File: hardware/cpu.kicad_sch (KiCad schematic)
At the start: 8 parts, among them U1 H3

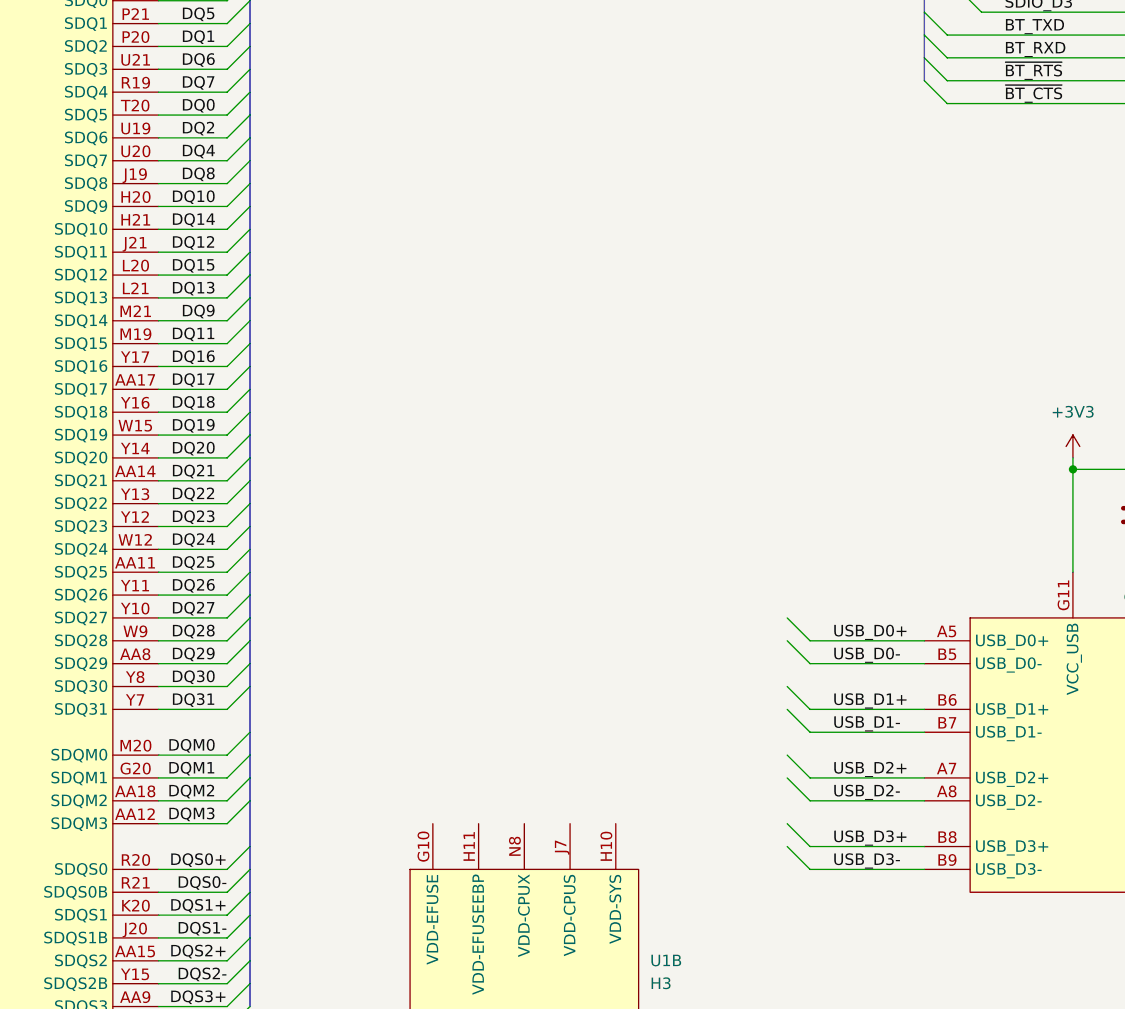
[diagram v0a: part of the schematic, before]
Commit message: Re-routed DDR3 on L4 & drew USB schematic
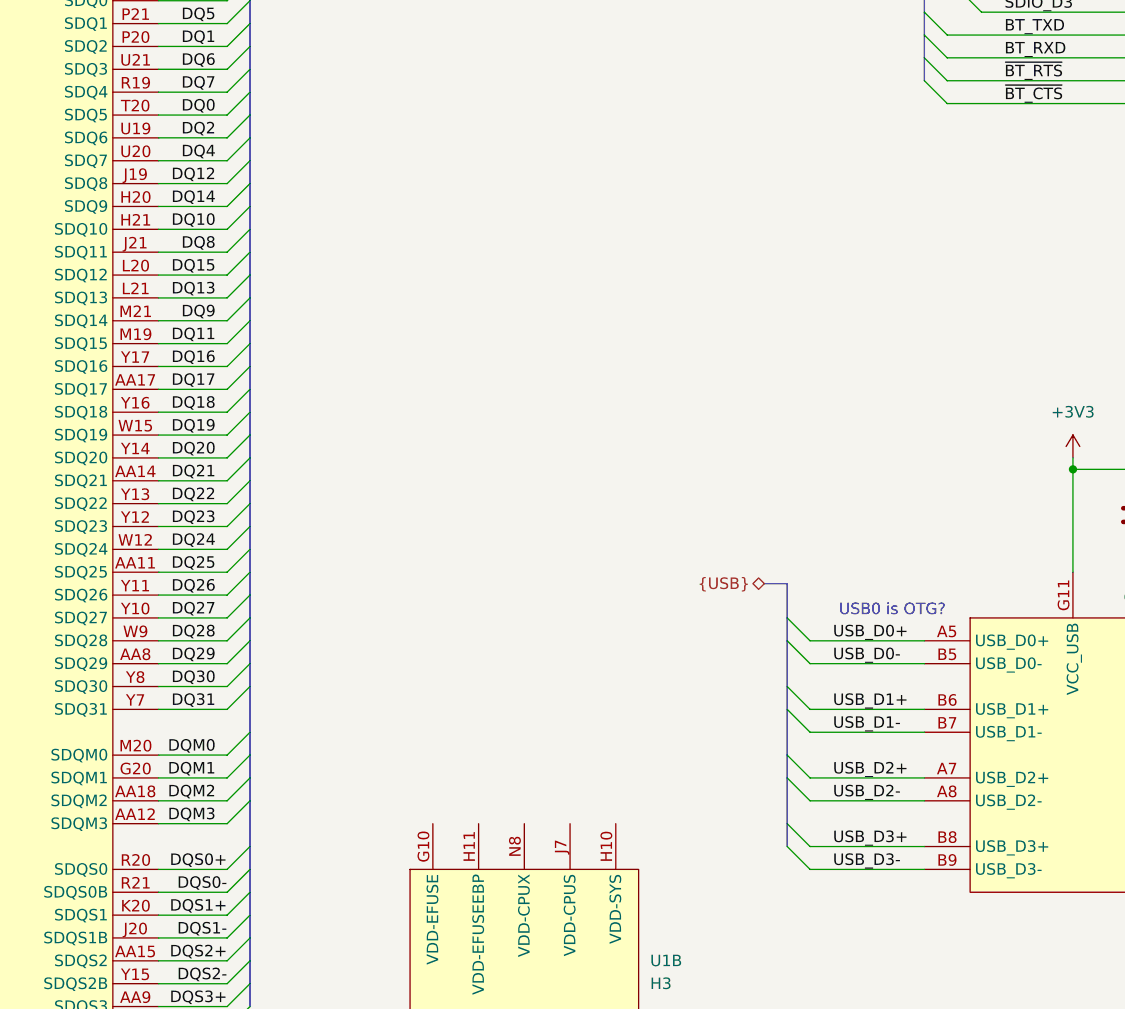
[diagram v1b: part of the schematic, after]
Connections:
- net DQ10: now also U1.H21 (SDQ10); no longer U1.H20 (SDQ9)
- net DQ12: now also U1.J19 (SDQ8); no longer U1.J21 (SDQ11)
- net DQ14: now also U1.H20 (SDQ9); no longer U1.H21 (SDQ10)
- net DQ8: now also U1.J21 (SDQ11); no longer U1.J19 (SDQ8)
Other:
- note added: "USB0 is OTG?"
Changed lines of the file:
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@@
 	(generator_version "9.0")
 	(paper "A4")
+	(text "USB0 is OTG?"
+		(exclude_from_sim no)
+		(at 184.404 121.158 0)
+		(effects
+			(font
+				(size 1.27 1.27)
+			)
+		)
+	)
 	(junction
 		(at 212.09 22.86)
@@
 		)
 	)
+	(bus
+		(pts
+			(xy 172.72 132.08) (xy 172.72 129.54)
+		)
+		(stroke
+			(width 0)
+			(type default)
+		)
+	)
 	(wire
 		(pts
@@
 		)
 	)
+	(bus
+		(pts
+			(xy 172.72 137.16) (xy 172.72 132.08)
+		)
+		(stroke
+			(width 0)
+			(type default)
+		)
+	)
 	(wire
 		(pts
@@
 		)
 	)
+	(bus
+		(pts
+			(xy 172.72 124.46) (xy 172.72 121.92)
+		)
+		(stroke
+			(width 0)
+			(type default)
+		)
+	)
 	(wire
 		(pts
@@
 		)
 	)
+	(bus
+		(pts
+			(xy 172.72 139.7) (xy 172.72 137.16)
+		)
+		(stroke
+			(width 0)
+			(type default)
+		)
+	)
 	(wire
 		(pts
@@
 		)
 	)
+	(bus
+		(pts
+			(xy 172.72 144.78) (xy 172.72 139.7)
+		)
+		(stroke
+			(width 0)
+			(type default)
+		)
+	)
+	(bus
+		(pts
+			(xy 172.72 121.92) (xy 172.72 118.11)
+		)
+		(stroke
+			(width 0)
+			(type default)
+		)
+	)
 	(wire
 		(pts
@@
 		)
 	)
+	(bus
+		(pts
+			(xy 172.72 118.11) (xy 170.18 118.11)
+		)
+		(stroke
+			(width 0)
+			(type default)
+		)
+	)
 	(wire
 		(pts
@@
 	(bus
 		(pts
+			(xy 172.72 147.32) (xy 172.72 144.78)
+		)
+		(stroke
+			(width 0)
+			(type default)
+		)
+	)
+	(bus
+		(pts
+			(xy 172.72 129.54) (xy 172.72 124.46)
+		)
+		(stroke
+			(width 0)
+			(type default)
+		)
+	)
+	(bus
+		(pts
 			(xy 113.03 63.5) (xy 113.03 60.96)
 		)
@@
 	)
 	(label "DQ12"
-		(at 109.22 81.28 180)
+		(at 109.22 73.66 180)
 		(effects
 			(font
@@
 	)
 	(label "DQ10"
-		(at 109.22 76.2 180)
+		(at 109.22 78.74 180)
 		(effects
 			(font
@@
 	)
 	(label "DQ14"
-		(at 109.22 78.74 180)
+		(at 109.22 76.2 180)
 		(effects
 			(font
@@
 	)
 	(label "DQ8"
-		(at 109.22 73.66 180)
+		(at 109.22 81.28 180)
 		(effects
 			(font
@@
 		)
 	)
+	(hierarchical_label "{USB}"
+		(shape bidirectional)
+		(at 170.18 118.11 180)
+		(effects
+			(font
+				(size 1.27 1.27)
+			)
+			(justify right)
+		)
+	)
 	(hierarchical_label "{DATA}"
 		(shape bidirectional)
@@
 		(on_board yes)
 		(dnp no)
-		(fields_autoplaced yes)
 		(property "Reference" "U1"
 			(at 217.17 135.8899 0)
